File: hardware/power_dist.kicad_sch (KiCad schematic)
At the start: 15 parts, among them U1 TPS62175DQC, U7 LT1962-3.3

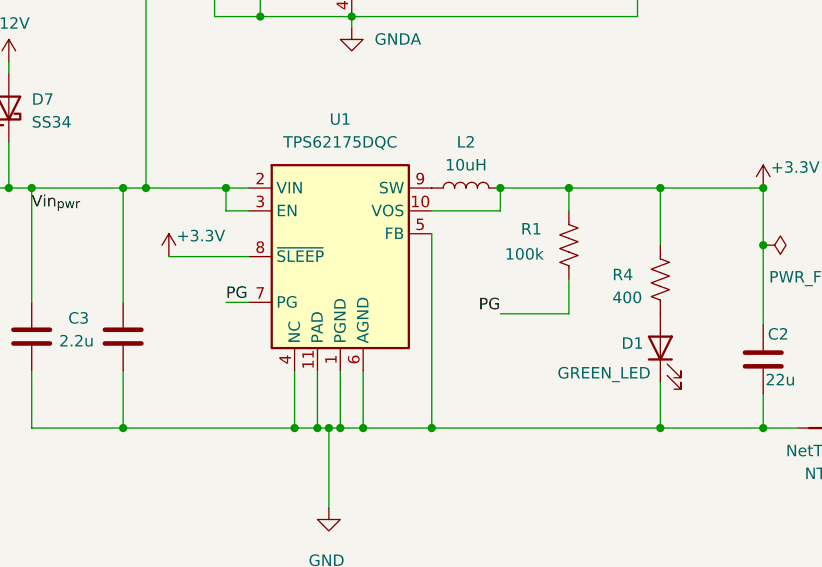
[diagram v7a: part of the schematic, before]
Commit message: tied PG to mcu reset
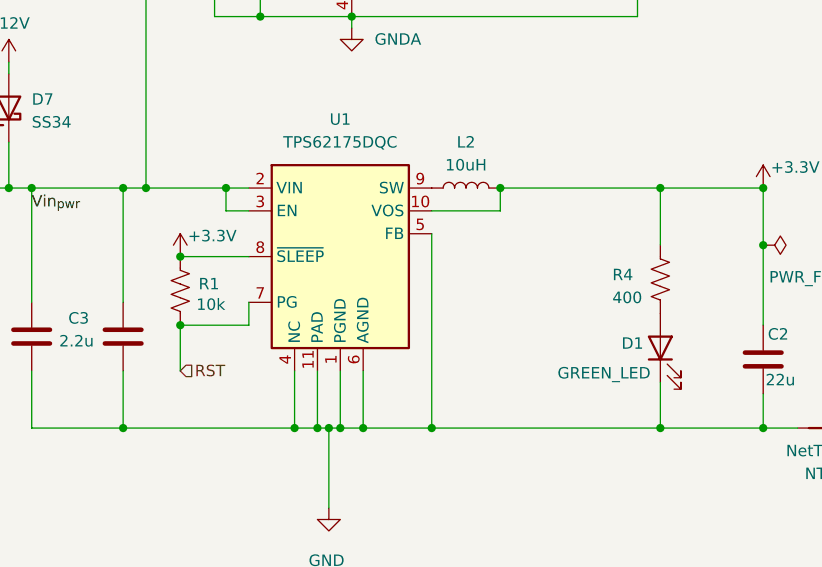
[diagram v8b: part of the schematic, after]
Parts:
- R1: value 100k -> 10k; LCSC C14675 -> C25804
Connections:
- net PG renamed RST
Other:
- moved on the sheet: R1
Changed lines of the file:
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@@
-	)
-	(junction
-		(at 132.08 58.42)
-		(diameter 0)
-		(color 0 0 0 0)
 	)
 	(junction
@@
 	)
 	(junction
+		(at 88.9 66.04)
+		(diameter 0)
+		(color 0 0 0 0)
+	)
+	(junction
 		(at 116.84 85.09)
 		(diameter 0)
@@
 	)
 	(junction
+		(at 88.9 73.66)
+		(diameter 0)
+		(color 0 0 0 0)
+	)
+	(junction
 		(at 124.46 58.42)
 		(diameter 0)
@@
 	(wire
 		(pts
-			(xy 124.46 72.39) (xy 132.08 72.39)
-		)
-		(stroke
-			(width 0)
-			(type default)
-		)
-	)
-	(wire
-		(pts
 			(xy 93.98 58.42) (xy 96.52 58.42)
 		)
@@
 	(wire
 		(pts
-			(xy 132.08 58.42) (xy 142.24 58.42)
+			(xy 124.46 58.42) (xy 142.24 58.42)
+		)
+		(stroke
+			(width 0)
+			(type default)
+		)
+	)
+	(wire
+		(pts
+			(xy 88.9 78.74) (xy 88.9 73.66)
 		)
 		(stroke
@@
 	(wire
 		(pts
-			(xy 132.08 72.39) (xy 132.08 68.58)
-		)
-		(stroke
-			(width 0)
-			(type default)
-		)
-	)
-	(wire
-		(pts
-			(xy 87.63 66.04) (xy 96.52 66.04)
+			(xy 88.9 66.04) (xy 96.52 66.04)
 		)
 		(stroke
@@
 	(wire
 		(pts
+			(xy 88.9 73.66) (xy 96.52 73.66)
+		)
+		(stroke
+			(width 0)
+			(type default)
+		)
+	)
+	(wire
+		(pts
 			(xy 105.41 85.09) (xy 105.41 93.98)
 		)
@@
 	(wire
 		(pts
-			(xy 124.46 58.42) (xy 132.08 58.42)
-		)
-		(stroke
-			(width 0)
-			(type default)
-		)
-	)
-	(wire
-		(pts
 			(xy 153.67 81.28) (xy 153.67 85.09)
 		)
@@
 	(wire
 		(pts
+			(xy 96.52 73.66) (xy 96.52 71.12)
+		)
+		(stroke
+			(width 0)
+			(type default)
+		)
+	)
+	(wire
+		(pts
 			(xy 82.55 78.74) (xy 82.55 85.09)
 		)
@@
 		(pts
 			(xy 104.14 85.09) (xy 105.41 85.09)
-		)
-		(stroke
-			(width 0)
-			(type default)
-		)
-	)
-	(wire
-		(pts
-			(xy 93.98 71.12) (xy 96.52 71.12)
-		)
-		(stroke
-			(width 0)
-			(type default)
-		)
-	)
-	(wire
-		(pts
-			(xy 132.08 60.96) (xy 132.08 58.42)
 		)
 		(stroke
@@
 		)
 	)
-	(label "PG"
-		(at 93.98 71.12 0)
+	(hierarchical_label "RST"
+		(shape input)
+		(at 88.9 78.74 0)
 		(effects
 			(font
 				(size 1.27 1.27)
 			)
-			(justify left bottom)
-		)
-	)
-	(label "PG"
-		(at 124.46 72.39 180)
-		(effects
-			(font
-				(size 1.27 1.27)
-			)
-			(justify right bottom)
+			(justify left)
 		)
 	)
@@
 	(symbol
 		(lib_id "power:+3.3V")
-		(at 87.63 66.04 0)
+		(at 88.9 66.04 0)
 		(unit 1)
 		(exclude_from_sim no)
@@
 		(dnp no)
 		(property "Reference" "#PWR025"
-			(at 87.63 69.85 0)
+			(at 88.9 69.85 0)
 			(effects
 				(font
@@
 		)
 		(property "Value" "+3.3V"
-			(at 91.186 63.754 0)
+			(at 92.456 63.754 0)
 			(effects
 				(font
@@
 		)
 		(property "Footprint" ""
-			(at 87.63 66.04 0)
+			(at 88.9 66.04 0)
 			(effects
 				(font
@@
 		)
 		(property "Datasheet" ""
-			(at 87.63 66.04 0)
+			(at 88.9 66.04 0)
 			(effects
 				(font
@@
 		)
 		(property "Description" "Power symbol creates a global label with name \"+3.3V\""
-			(at 87.63 66.04 0)
+			(at 88.9 66.04 0)
 			(effects
 				(font
@@
 	(symbol
 		(lib_id "Device:R_US")
-		(at 132.08 64.77 0)
+		(at 88.9 69.85 0)
 		(unit 1)
 		(exclude_from_sim no)
@@
 		(dnp no)
 		(property "Reference" "R1"
-			(at 126.746 62.992 0)
+			(at 90.932 69.088 0)
 			(effects
 				(font
@@
 			)
 		)
-		(property "Value" "100k"
-			(at 124.968 65.786 0)
+		(property "Value" "10k"
+			(at 90.678 71.374 0)
 			(effects
 				(font
@@
 		)
 		(property "Footprint" "Resistor_SMD:R_0603_1608Metric"
-			(at 133.096 65.024 90)
+			(at 89.916 70.104 90)
 			(effects
 				(font
@@
 		)
 		(property "Datasheet" "~"
-			(at 132.08 64.77 0)
+			(at 88.9 69.85 0)
 			(effects
 				(font
@@
 		)
 		(property "Description" "Resistor, US symbol"
-			(at 132.08 64.77 0)
-			(effects
-				(font
-					(size 1.27 1.27)
-				)
-				(hide yes)
-			)
-		)
-		(property "LCSC" "C14675"
-			(at 132.08 64.77 0)
-			(effects
-				(font
+			(at 88.9 69.85 0)
+			(effects
+				(font
+					(size 1.27 1.27)
+				)
+				(hide yes)
+			)
+		)
+		(property "LCSC" "C25804"
+			(at 88.9 69.85 0)
+			(effects
+				(font
